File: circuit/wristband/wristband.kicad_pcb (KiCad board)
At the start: 4 copper layers, 47 x 70 mm, 84 parts, among them IC1 LT6230CS6, IC2 LT6230CS6, IC3 LT6230CS6, IC4 LT6230CS6, IC5 LT6230CS6, IC6 LT6230CS6

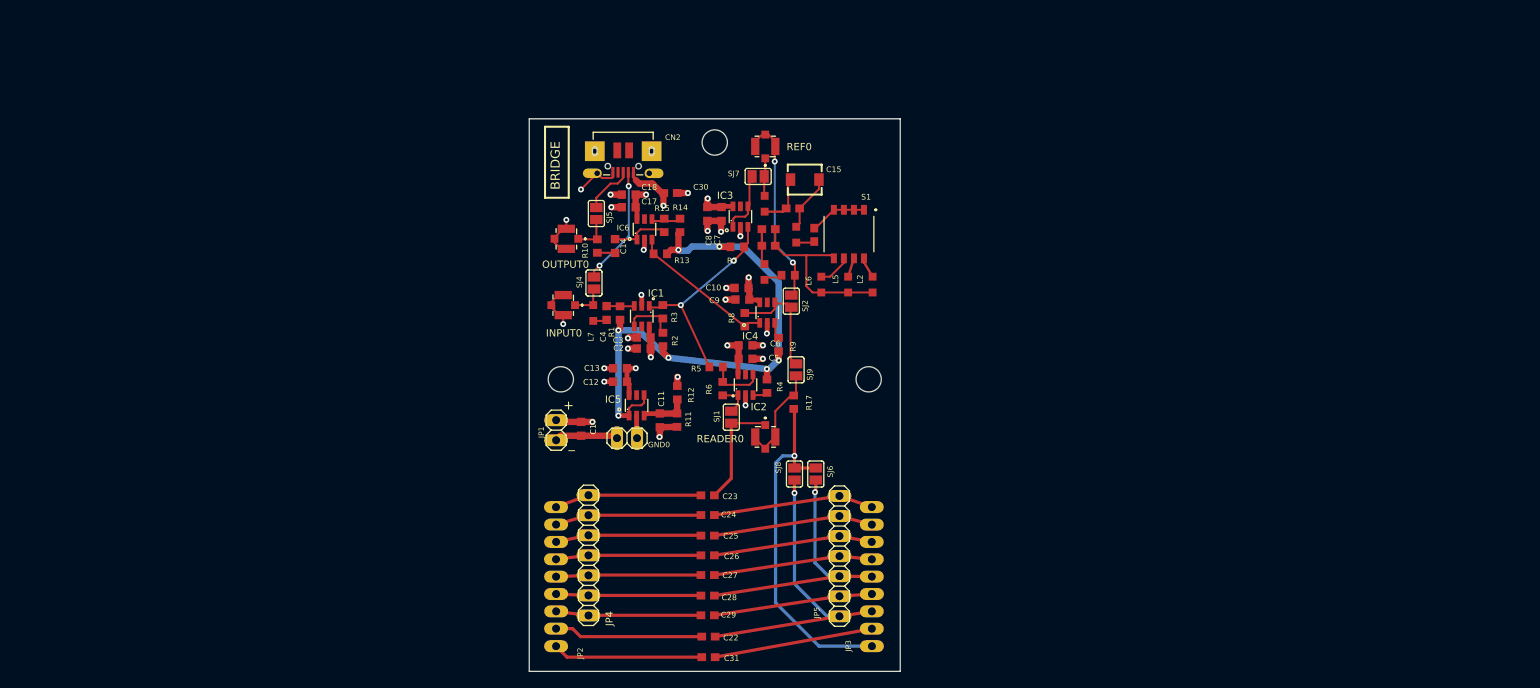
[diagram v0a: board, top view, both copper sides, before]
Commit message: add wristband
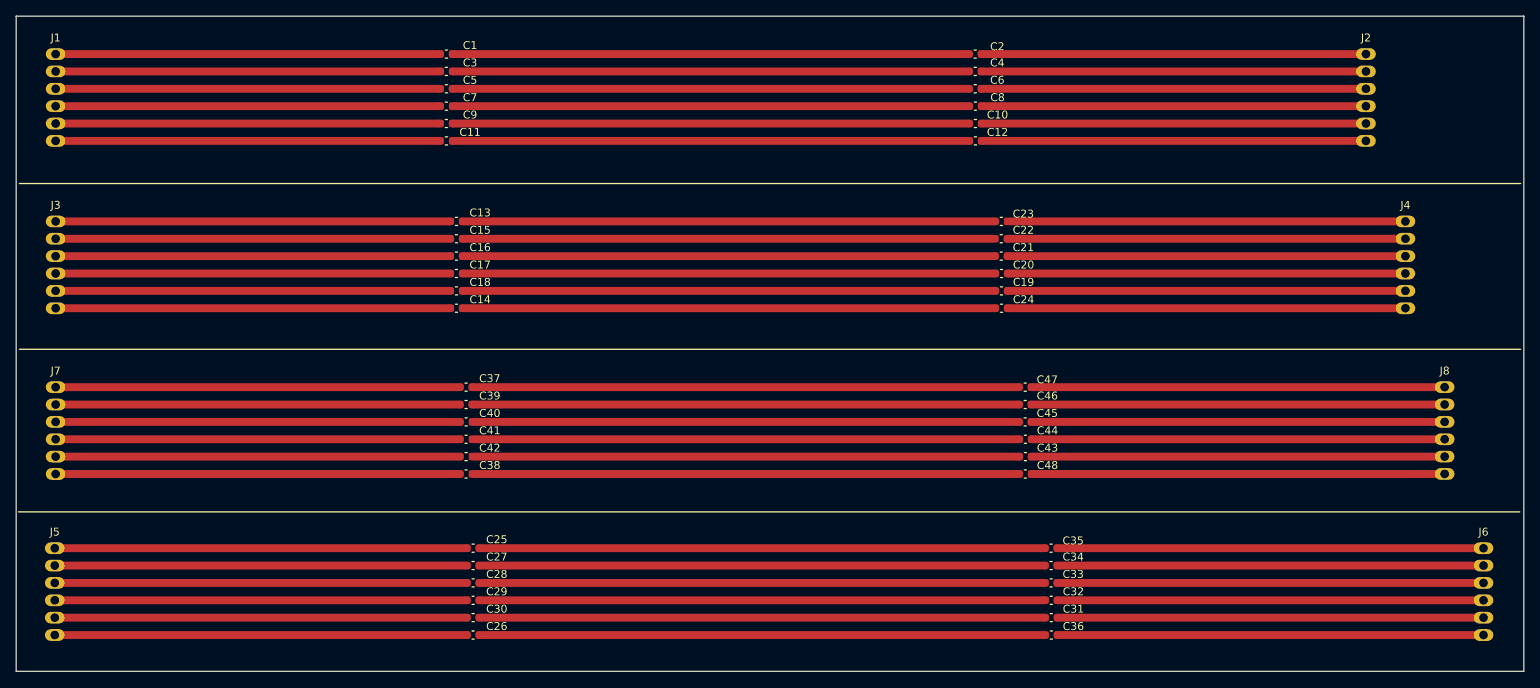
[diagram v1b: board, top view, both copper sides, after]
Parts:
- removed @HOLE0, @HOLE1, @HOLE2: , 
- removed CN2: , 4UCONN_20329
- removed GND0, JP1: , 1X02_325
- removed IC1, IC2, IC3, IC4, IC5, IC6: LT6230CS6, TSOT23-6_261
- removed INPUT0, OUTPUT0, READER0, REF0: 0734120114, 0734120114
- removed JP2, JP3: , 1X09
- removed JP4, JP5: , 1X07_325
- removed L1, L3, L4, L7: , L2012C_334
- removed L2: 0.2u, L2012C_334
- removed L5: 0.15u, L2012C_334
- removed L6: 0.1u, L2012C_334
- removed R1, R10, R4: 50, R0603_334
- removed R11, R12: 10k, R0603_334
- removed R13, R14, R15, R2, R3, R5, R6, R7, R8: 100, R0603_334
- removed R16, R17: , R0603_334
- removed R9: 0, R0603_334
- removed S1: KAN1104RT, KAN1104RT
- removed SJ1, SJ2, SJ4, SJ5, SJ6, SJ7, SJ8, SJ9: , SJ_252
- added C32: C, Capacitor_SMD:C_0603_1608Metric, F.Cu at (191.1, 131.0)
- added C33: C, Capacitor_SMD:C_0603_1608Metric, F.Cu at (191.1, 128.8)
- added C34: C, Capacitor_SMD:C_0603_1608Metric, F.Cu at (191.1, 126.6)
- added C35: C, Capacitor_SMD:C_0603_1608Metric, F.Cu at (191.1, 124.4)
- added C36: C, Capacitor_SMD:C_0603_1608Metric, F.Cu at (191.1, 135.4)
- added C37: C, Capacitor_SMD:C_0603_1608Metric, F.Cu at (117.0, 104.0)
- added C38: C, Capacitor_SMD:C_0603_1608Metric, F.Cu at (117.0, 115.0)
- added C39: C, Capacitor_SMD:C_0603_1608Metric, F.Cu at (117.0, 106.2)
- added C40: C, Capacitor_SMD:C_0603_1608Metric, F.Cu at (117.0, 108.4)
- added C41: C, Capacitor_SMD:C_0603_1608Metric, F.Cu at (117.0, 110.6)
- added C42: C, Capacitor_SMD:C_0603_1608Metric, F.Cu at (117.0, 112.8)
- added C43: C, Capacitor_SMD:C_0603_1608Metric, F.Cu at (187.9, 112.8)
- added C44: C, Capacitor_SMD:C_0603_1608Metric, F.Cu at (187.9, 110.6)
- added C45: C, Capacitor_SMD:C_0603_1608Metric, F.Cu at (187.8, 108.4)
- added C46: C, Capacitor_SMD:C_0603_1608Metric, F.Cu at (187.8, 106.2)
- added C47: C, Capacitor_SMD:C_0603_1608Metric, F.Cu at (187.8, 104.0)
- added C48: C, Capacitor_SMD:C_0603_1608Metric, F.Cu at (187.9, 115.0)
- added J1: Conn_01x06_Pin, Connector_PinHeader_2.00mm:PinHeader_1x06_P2.00mm_Vertical, F.Cu at (65.0, 61.8)
- added J2: Conn_01x06_Pin, Connector_PinHeader_2.00mm:PinHeader_1x06_P2.00mm_Vertical, F.Cu at (231.0, 61.8)
- added J3: Conn_01x06_Pin, Connector_PinHeader_2.00mm:PinHeader_1x06_P2.00mm_Vertical, F.Cu at (65.0, 83.0)
- added J4: Conn_01x06_Pin, Connector_PinHeader_2.00mm:PinHeader_1x06_P2.00mm_Vertical, F.Cu at (236.0, 83.0)
- added J5: Conn_01x06_Pin, Connector_PinHeader_2.00mm:PinHeader_1x06_P2.00mm_Vertical, F.Cu at (64.9, 124.4)
- added J6: Conn_01x06_Pin, Connector_PinHeader_2.00mm:PinHeader_1x06_P2.00mm_Vertical, F.Cu at (245.9, 124.4)
- added J7: Conn_01x06_Pin, Connector_PinHeader_2.00mm:PinHeader_1x06_P2.00mm_Vertical, F.Cu at (65.0, 104.0)
- added J8: Conn_01x06_Pin, Connector_PinHeader_2.00mm:PinHeader_1x06_P2.00mm_Vertical, F.Cu at (241.0, 104.0)
- C1: value 10u -> C; footprint C0603K_334 -> Capacitor_SMD:C_0603_1608Metric
- C10, C13, C18, C3, C6, C8: value 1.0u -> C; footprint C0603K_334 -> Capacitor_SMD:C_0603_1608Metric
- C11, C12, C17, C2, C5, C7, C9: value 0.1u -> C; footprint C0603K_334 -> Capacitor_SMD:C_0603_1608Metric
- C14: value (none) -> C; footprint C0603K_334 -> Capacitor_SMD:C_0603_1608Metric
- C15: value (none) -> C; footprint CTRIMTZBX4_334 -> Capacitor_SMD:C_0603_1608Metric
- C16, C19, C20, C21, C22, C23, C24, C25, C26, C27, C28, C29, C30, C31: value (none) -> C; footprint C1608_334 -> Capacitor_SMD:C_0603_1608Metric
- C4: value 120p -> C; footprint C0603K_334 -> Capacitor_SMD:C_0603_1608Metric
- moved C22 62.6 mm to (184.8, 85.2)
- moved C30 59.3 mm to (117.9, 133.2)
- moved C2 56.2 mm to (181.5, 61.8), turned to 0 degrees
- moved C4 55.8 mm to (181.5, 64.0), turned to 0 degrees
- moved C12 54.4 mm to (181.5, 72.8), turned to 0 degrees
- moved C5 51.1 mm to (114.5, 66.2)
- moved C23 50.9 mm to (184.8, 83.0)
- moved C1 50.5 mm to (114.5, 61.8), turned to 0 degrees
- moved C24 45.5 mm to (184.8, 94.0)
- moved C16 45.4 mm to (115.8, 87.4), turned to 0 degrees
- moved C15 44.8 mm to (115.8, 85.2), turned to 0 degrees
- moved C11 44.6 mm to (114.5, 72.8), turned to 0 degrees
- moved C31 43.7 mm to (191.1, 133.2)
- moved C9 43.6 mm to (114.5, 70.6), turned to 0 degrees
- moved C6 43.6 mm to (181.5, 66.2)
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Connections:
- C1 pad 1: VCC -> Net-(J1-Pin_1)
- C1 pad 2: GND -> Net-(C1-Pad2)
- C10 pad 1: VCC -> Net-(C10-Pad1)
- C10 pad 2: GND -> Net-(J2-Pin_5)
- C11 pad 2: GND -> Net-(C11-Pad2)
- C12 pad 1: VCC -> Net-(C11-Pad2)
- C12 pad 2: GND -> Net-(J2-Pin_6)
- C13 pad 1: VCC -> Net-(J3-Pin_1)
- C13 pad 2: GND -> Net-(C13-Pad2)
- C14 pad 2: N$5 -> Net-(C14-Pad2)
- C15 pad 1: N$22 -> Net-(J3-Pin_2)
- C15 pad 2: N$21 -> Net-(C15-Pad2)
- C16 pad 2: N$9 -> Net-(C16-Pad2)
- C17 pad 1: VCC -> Net-(J3-Pin_4)
- C17 pad 2: GND -> Net-(C17-Pad2)
- C18 pad 1: VCC -> Net-(J3-Pin_5)
- C18 pad 2: GND -> Net-(C18-Pad2)
- C19 pad 1: N$52 -> Net-(C18-Pad2)
- C19 pad 2: N$51 -> Net-(J4-Pin_5)
- C2 pad 1: VCC -> Net-(C1-Pad2)
- C2 pad 2: GND -> Net-(J2-Pin_1)
- C20 pad 1: N$52 -> Net-(C17-Pad2)
- C20 pad 2: N$51 -> Net-(J4-Pin_4)
- C21 pad 1: N$22 -> Net-(C16-Pad2)
- C21 pad 2: N$21 -> Net-(J4-Pin_3)
- C22 pad 1: N$3 -> Net-(C15-Pad2)
- C23 pad 1: N$10 -> Net-(C13-Pad2)
- C24 pad 1: N$27 -> Net-(C14-Pad2)
- C3 pad 1: VCC -> Net-(J1-Pin_2)
- C3 pad 2: GND -> Net-(C3-Pad2)
- C30 pad 1: VCC -> Net-(J5-Pin_5)
- C30 pad 2: GND -> Net-(C30-Pad2)
- C31 pad 1: N$44 -> Net-(C30-Pad2)
- C4 pad 1: N$39 -> Net-(C3-Pad2)
- C5 pad 1: VCC -> Net-(J1-Pin_3)
- C5 pad 2: GND -> Net-(C5-Pad2)
- C6 pad 1: VCC -> Net-(C5-Pad2)
- C6 pad 2: GND -> Net-(J2-Pin_3)
- C7 pad 1: VCC -> Net-(J1-Pin_4)
- C7 pad 2: GND -> Net-(C7-Pad2)
- C8 pad 1: VCC -> Net-(C7-Pad2)
- C8 pad 2: GND -> Net-(J2-Pin_4)
- C9 pad 1: VCC -> Net-(J1-Pin_5)
- C9 pad 2: GND -> Net-(C10-Pad1)
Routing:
- net VCC/2: track 74.4 -> 0.00 mm, vias 7 -> 0
- net Net-(C30-Pad2): track 0.00 -> 71.7 mm
- net Net-(C39-Pad2): track 0.00 -> 69.3 mm
- net Net-(C37-Pad2): track 0.00 -> 69.3 mm
- net Net-(C42-Pad2): track 0.00 -> 69.1 mm
- net Net-(C41-Pad2): track 0.00 -> 69.1 mm
- net Net-(C40-Pad2): track 0.00 -> 69.1 mm
- net Net-(C38-Pad2): track 0.00 -> 69.1 mm
- net Net-(C18-Pad2): track 0.00 -> 67.5 mm
- net Net-(C17-Pad2): track 0.00 -> 67.5 mm
- net Net-(C14-Pad2): track 0.00 -> 67.5 mm
- net Net-(C16-Pad2): track 0.00 -> 67.5 mm
- net Net-(C13-Pad2): track 0.00 -> 67.5 mm
- net Net-(C15-Pad2): track 0.00 -> 67.2 mm
- net Net-(C7-Pad2): track 0.00 -> 65.5 mm
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- removed copper zone on In1.Cu, net GND
- removed copper zone on In2.Cu, net VCC
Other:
- board size 47 x 70 mm -> 191 x 83 mm
- copper layers 4 -> 2
- board text added: "Please fill the area between the two rectangles with stiffener"
- board text removed: "+"
- board text removed: "BRIDGE"
- board text removed: "_"
